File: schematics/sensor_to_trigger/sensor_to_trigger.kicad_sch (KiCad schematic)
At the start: 6 parts, among them J1 Conn_01x03_Female, J2 Conn_01x05_Male, Q1 2N3904

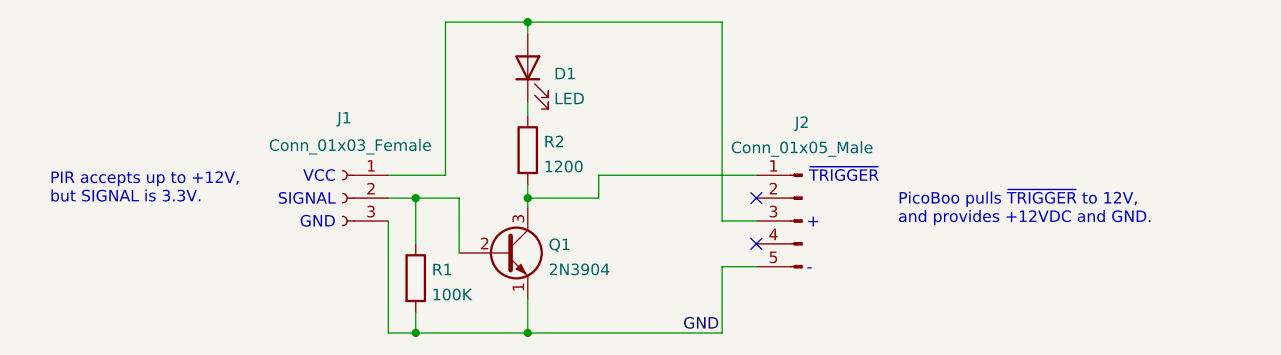
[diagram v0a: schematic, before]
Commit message: Improved notes on PIR-to-trigger schematic.
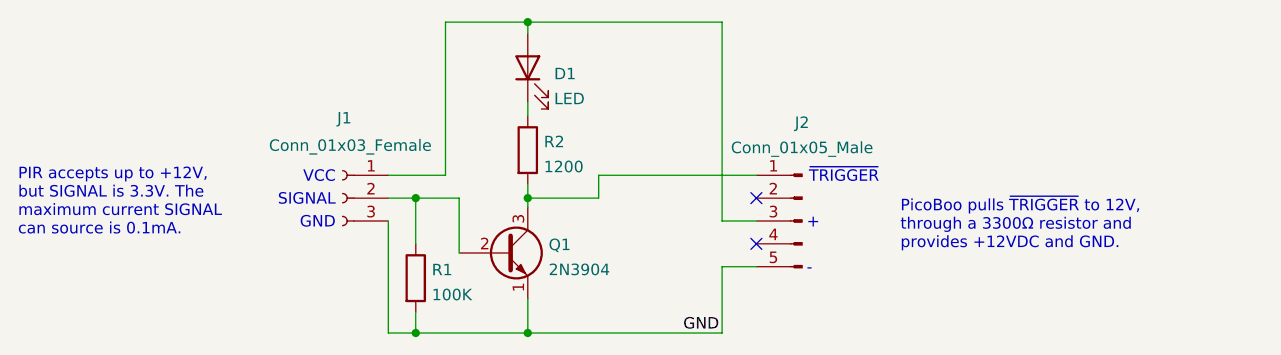
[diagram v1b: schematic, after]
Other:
- note added: "PIR accepts up to +12V, but SIGNAL is 3.3V. The maximum current SIGNAL can source is 0.1mA."
- note added: "PicoBoo pulls ~{TRIGGER} to 12V, through a 3300Ω resistor and provides +12VDC and GND."
- note removed: "PIR accepts up to +12V, but SIGNAL is 3.3V."
- note removed: "PicoBoo pulls ~{TRIGGER} to 12V, and provides +12VDC and GND."
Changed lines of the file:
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@@
     (effects (font (size 1.27 1.27)) (justify right bottom))
   )
-  (text "PicoBoo pulls ~{TRIGGER} to 12V,\nand provides +12VDC and GND.\n"
-    (at 186.944 104.648 0)
+  (text "PicoBoo pulls ~{TRIGGER} to 12V,\nthrough a 3300Ω resistor and\nprovides +12VDC and GND.\n"
+    (at 187.198 107.442 0)
     (effects (font (size 1.27 1.27)) (justify left bottom))
   )
@@
     (effects (font (size 1.27 1.27)) (justify right bottom))
   )
-  (text "PIR accepts up to +12V,\nbut SIGNAL is 3.3V." (at 92.71 102.362 0)
+  (text "PIR accepts up to +12V,\nbut SIGNAL is 3.3V. The\nmaximum current SIGNAL\ncan source is 0.1mA."
+    (at 89.154 105.918 0)
     (effects (font (size 1.27 1.27)) (justify left bottom))
   )
